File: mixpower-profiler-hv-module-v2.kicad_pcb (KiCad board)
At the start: 2 copper layers, 56.7 x 45.7 mm, 71 parts, among them J1 VIN_TERMINAL, J2 VIN_HEADERS, J3 COMM_HEADERS, J3_CASTELLATIONS COMM_HEADERS, Q1 STL130N6F7, Q2 STL130N6F7, Q3 STL130N6F7, Q4 STL130N6F7, Q5 STL130N6F7, Q6 STL130N6F7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

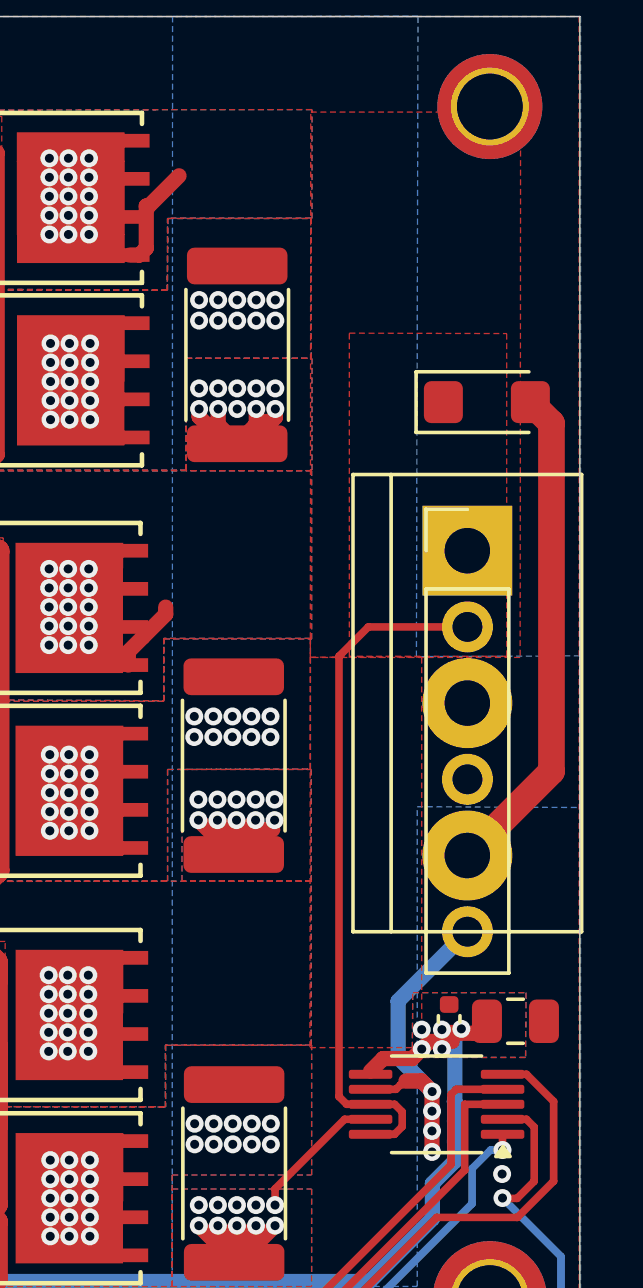
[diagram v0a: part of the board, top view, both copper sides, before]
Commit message: feat: add PTC fuse on VIN
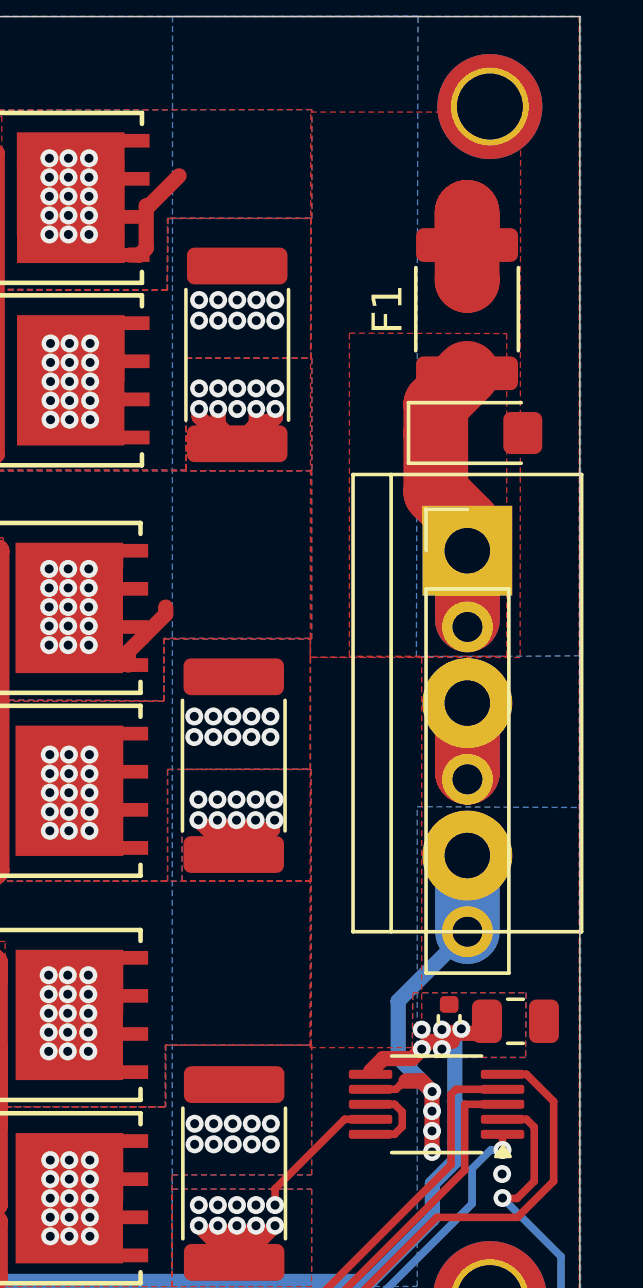
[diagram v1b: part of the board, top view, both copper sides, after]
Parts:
- added F1: Polyfuse_Small, Resistor_SMD:R_1812_4532Metric, F.Cu at (229.4, 56.7)
- moved D7 1.06 mm to (229.8, 60.9)
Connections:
- D7 pad 1: /VIN_P -> /VIN_P_IN
- J1 pad 1: /VIN_P -> /VIN_P_IN
- J2 pad 1: /VIN_P -> /VIN_P_IN
- J2 pad 2: /VIN_P -> /VIN_P_IN
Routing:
- net /VIN_P: track 29.3 -> 12.2 mm
- net GND: track 50.1 -> 36.1 mm
- net /VIN_P_IN: track 0.00 -> 13.9 mm
- net /VIN_N: track 24.0 -> 31.2 mm
